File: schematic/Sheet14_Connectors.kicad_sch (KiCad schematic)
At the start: 5 parts, among them J1 JTAG, J2 SPW_TX, J3 SPW_RX, J4 POWER, J5 UART

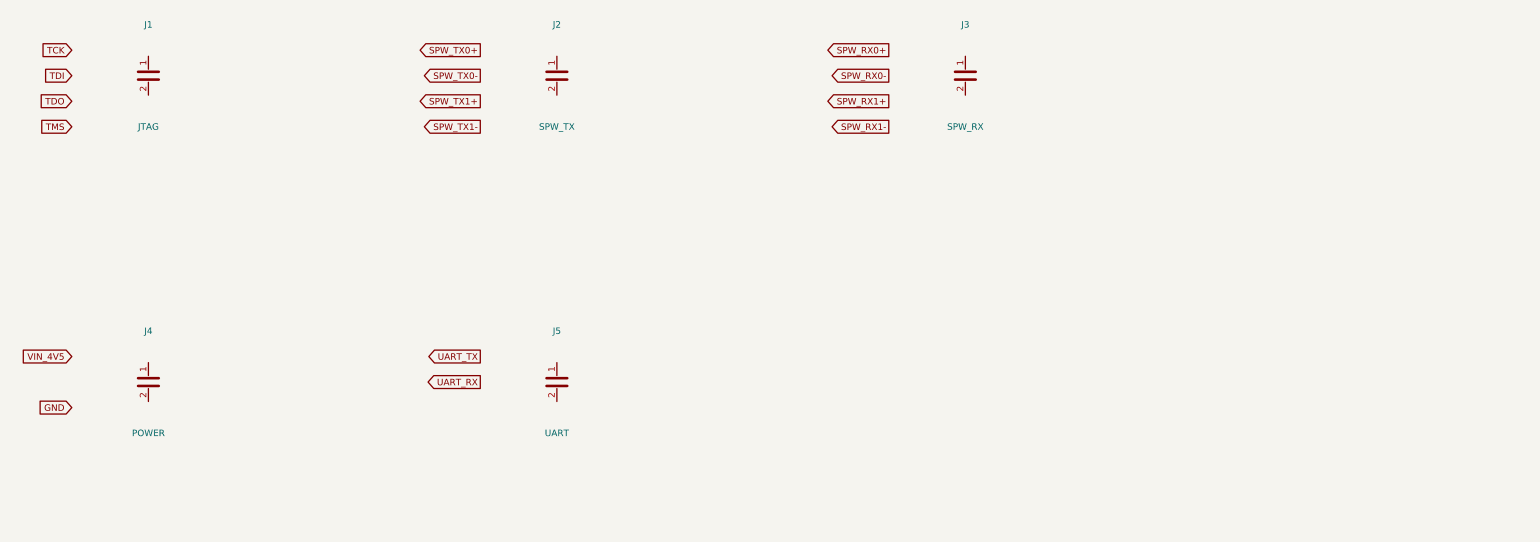
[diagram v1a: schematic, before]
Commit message: feat: schematic sheets with datasheet-correct IC pinouts and connections
- Downloaded 10 official datasheets (TI, Renesas, Crystek) for all major ICs
- Extracted exact pin configurations from PDF pin tables
- Generated Custom_ICs.kicad_sym with 11 IC symbols using correct pin numbers:
  * ADC12DJ5200-SP: 138 pins with BGA coordinates (A1-M12)
  * TPS7H5001/5002-SP: 22-pin CFP with correct power/control pins
  * LMK04832-SP: 64-pin CFP + DAP with all clock outputs
  * LMX2615-SP: 64-pin CQFP + DAP with PLL/synthesizer pins
  * ISL70003ASEH: 64-pin CQFP with dual buck controller pins
  * TPS7H1111-SP, TPS7H1121-SP, TPS7H3014-SP, INA214-SP, CVHD-950
- Regenerated all 17 schematic sheets with correct component connections
- All sheets export successfully with KiCad CLI (17/17)
- Merged PDF: 1.3MB, 17 pages
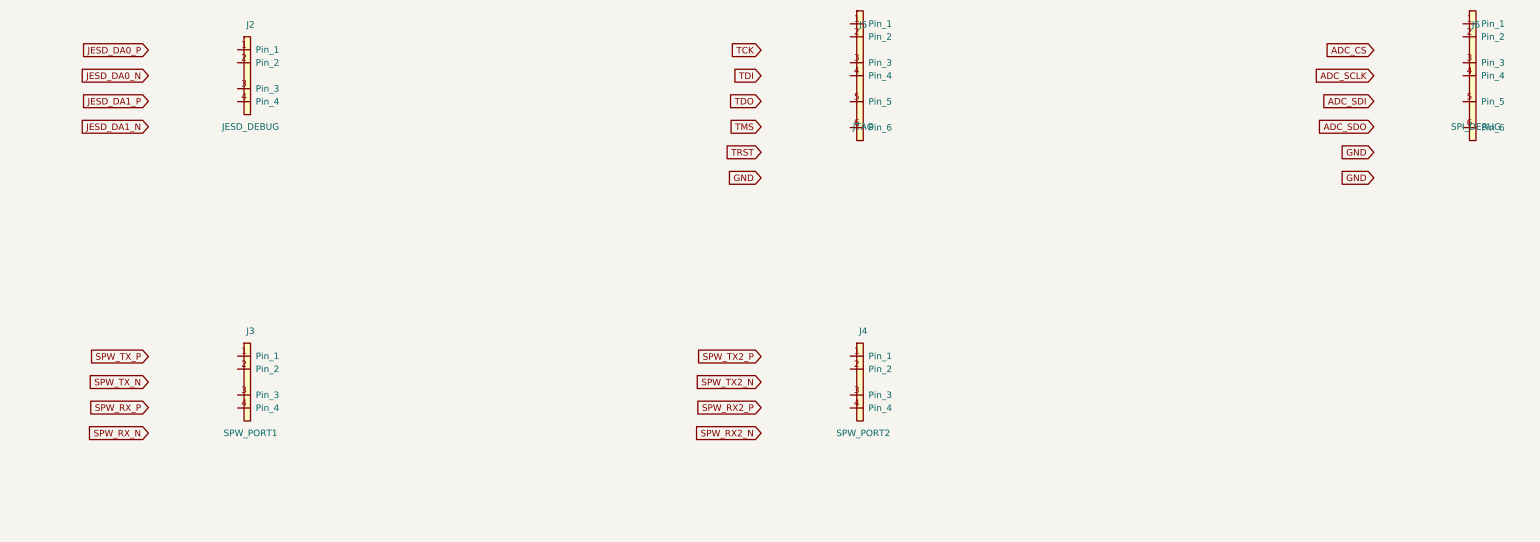
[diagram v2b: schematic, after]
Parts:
- removed J1: JTAG, Conn_01x06, symbol Device:C
- removed J2: SPW_TX, Conn_01x04, symbol Device:C
- removed J3: SPW_RX, Conn_01x04, symbol Device:C
- removed J4: POWER, Conn_01x02, symbol Device:C
- removed J5: UART, Conn_01x04, symbol Device:C
- added J2: JESD_DEBUG, Conn_01x04, symbol Connector:Conn_01x04
- added J3: SPW_PORT1, Conn_01x04, symbol Connector:Conn_01x04
- added J4: SPW_PORT2, Conn_01x04, symbol Connector:Conn_01x04
- added J5: JTAG, Conn_01x06, symbol Connector:Conn_01x06
- added J6: SPI_DEBUG, Conn_01x06, symbol Connector:Conn_01x06
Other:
- title: X-Band Digital Module 20x20cm -> X-Band Connectors
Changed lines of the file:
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@@
   (paper "A3")
   (title_block
-    (title "X-Band Digital Module 20x20cm")
+    (title "X-Band Connectors")
     (date "2026-09-10")
     (rev "1.0")
   )
-  (symbol (lib_id "Device:C") (at 60 60 0) (unit 1)
+  (symbol (lib_id "Connector:Conn_01x04") (at 80 60 0) (unit 1)
     (in_bom yes) (on_board yes)
-    (property "Reference" "J1" (at 60 50 0) (effects (font (size 1.27 1.27))))
-    (property "Value" "JTAG" (at 60 70 0) (effects (font (size 1.27 1.27))))
-    (property "Footprint" "Conn_01x06" (at 60 60 0) (effects (font (size 1.27 1.27)) hide))
+    (property "Reference" "J2" (at 80 50 0) (effects (font (size 1.27 1.27))))
+    (property "Value" "JESD_DEBUG" (at 80 70 0) (effects (font (size 1.27 1.27))))
+    (property "Footprint" "Conn_01x04" (at 80 60 0) (effects (font (size 1.27 1.27)) hide))
     (pin "1")
     (pin "2")
-  )
-  (symbol (lib_id "Device:C") (at 140 60 0) (unit 1)
+    (pin "3")
+    (pin "4")
+  )  (symbol (lib_id "Connector:Conn_01x04") (at 80 120 0) (unit 1)
     (in_bom yes) (on_board yes)
-    (property "Reference" "J2" (at 140 50 0) (effects (font (size 1.27 1.27))))
-    (property "Value" "SPW_TX" (at 140 70 0) (effects (font (size 1.27 1.27))))
-    (property "Footprint" "Conn_01x04" (at 140 60 0) (effects (font (size 1.27 1.27)) hide))
+    (property "Reference" "J3" (at 80 110 0) (effects (font (size 1.27 1.27))))
+    (property "Value" "SPW_PORT1" (at 80 130 0) (effects (font (size 1.27 1.27))))
+    (property "Footprint" "Conn_01x04" (at 80 120 0) (effects (font (size 1.27 1.27)) hide))
     (pin "1")
     (pin "2")
-  )
-  (symbol (lib_id "Device:C") (at 220 60 0) (unit 1)
+    (pin "3")
+    (pin "4")
+  )  (symbol (lib_id "Connector:Conn_01x04") (at 200 120 0) (unit 1)
     (in_bom yes) (on_board yes)
-    (property "Reference" "J3" (at 220 50 0) (effects (font (size 1.27 1.27))))
-    (property "Value" "SPW_RX" (at 220 70 0) (effects (font (size 1.27 1.27))))
-    (property "Footprint" "Conn_01x04" (at 220 60 0) (effects (font (size 1.27 1.27)) hide))
+    (property "Reference" "J4" (at 200 110 0) (effects (font (size 1.27 1.27))))
+    (property "Value" "SPW_PORT2" (at 200 130 0) (effects (font (size 1.27 1.27))))
+    (property "Footprint" "Conn_01x04" (at 200 120 0) (effects (font (size 1.27 1.27)) hide))
     (pin "1")
     (pin "2")
-  )
-  (symbol (lib_id "Device:C") (at 60 120 0) (unit 1)
+    (pin "3")
+    (pin "4")
+  )  (symbol (lib_id "Connector:Conn_01x06") (at 200 60 0) (unit 1)
     (in_bom yes) (on_board yes)
-    (property "Reference" "J4" (at 60 110 0) (effects (font (size 1.27 1.27))))
-    (property "Value" "POWER" (at 60 130 0) (effects (font (size 1.27 1.27))))
-    (property "Footprint" "Conn_01x02" (at 60 120 0) (effects (font (size 1.27 1.27)) hide))
+    (property "Reference" "J5" (at 200 50 0) (effects (font (size 1.27 1.27))))
+    (property "Value" "JTAG" (at 200 70 0) (effects (font (size 1.27 1.27))))
+    (property "Footprint" "Conn_01x06" (at 200 60 0) (effects (font (size 1.27 1.27)) hide))
     (pin "1")
     (pin "2")
-  )
-  (symbol (lib_id "Device:C") (at 140 120 0) (unit 1)
+    (pin "3")
+    (pin "4")
+    (pin "5")
+    (pin "6")
+  )  (symbol (lib_id "Connector:Conn_01x06") (at 320 60 0) (unit 1)
     (in_bom yes) (on_board yes)
-    (property "Reference" "J5" (at 140 110 0) (effects (font (size 1.27 1.27))))
-    (property "Value" "UART" (at 140 130 0) (effects (font (size 1.27 1.27))))
-    (property "Footprint" "Conn_01x04" (at 140 120 0) (effects (font (size 1.27 1.27)) hide))
+    (property "Reference" "J6" (at 320 50 0) (effects (font (size 1.27 1.27))))
+    (property "Value" "SPI_DEBUG" (at 320 70 0) (effects (font (size 1.27 1.27))))
+    (property "Footprint" "Conn_01x06" (at 320 60 0) (effects (font (size 1.27 1.27)) hide))
     (pin "1")
     (pin "2")
-  )
-  (global_label "TCK" (shape input) (at 45 55 180) (effects (font (size 1.27 1.27)) (justify right)))
-  (global_label "TDI" (shape input) (at 45 60 180) (effects (font (size 1.27 1.27)) (justify right)))
-  (global_label "TDO" (shape input) (at 45 65 180) (effects (font (size 1.27 1.27)) (justify right)))
-  (global_label "TMS" (shape input) (at 45 70 180) (effects (font (size 1.27 1.27)) (justify right)))
-  (global_label "SPW_TX0+" (shape output) (at 125 55 180) (effects (font (size 1.27 1.27)) (justify right)))
-  (global_label "SPW_TX0-" (shape output) (at 125 60 180) (effects (font (size 1.27 1.27)) (justify right)))
-  (global_label "SPW_TX1+" (shape output) (at 125 65 180) (effects (font (size 1.27 1.27)) (justify right)))
-  (global_label "SPW_TX1-" (shape output) (at 125 70 180) (effects (font (size 1.27 1.27)) (justify right)))
-  (global_label "SPW_RX0+" (shape output) (at 205 55 180) (effects (font (size 1.27 1.27)) (justify right)))
-  (global_label "SPW_RX0-" (shape output) (at 205 60 180) (effects (font (size 1.27 1.27)) (justify right)))
-  (global_label "SPW_RX1+" (shape output) (at 205 65 180) (effects (font (size 1.27 1.27)) (justify right)))
-  (global_label "SPW_RX1-" (shape output) (at 205 70 180) (effects (font (size 1.27 1.27)) (justify right)))
-  (global_label "VIN_4V5" (shape input) (at 45 115 180) (effects (font (size 1.27 1.27)) (justify right)))
-  (global_label "GND" (shape input) (at 45 125 180) (effects (font (size 1.27 1.27)) (justify right)))
-  (global_label "UART_TX" (shape output) (at 125 115 180) (effects (font (size 1.27 1.27)) (justify right)))
-  (global_label "UART_RX" (shape output) (at 125 120 180) (effects (font (size 1.27 1.27)) (justify right)))
-  (sheet_instances (path "/" (page "1")))
+    (pin "3")
+    (pin "4")
+    (pin "5")
+    (pin "6")
+  )  (global_label "JESD_DA0_P" (shape input) (at 60 55 180) (effects (font (size 1.27 1.27)) (justify right)))  (global_label "JESD_DA0_N" (shape input) (at 60 60 180) (effects (font (size 1.27 1.27)) (justify right)))  (global_label "JESD_DA1_P" (shape input) (at 60 65 180) (effects (font (size 1.27 1.27)) (justify right)))  (global_label "JESD_DA1_N" (shape input) (at 60 70 180) (effects (font (size 1.27 1.27)) (justify right)))  (global_label "SPW_TX_P" (shape input) (at 60 115 180) (effects (font (size 1.27 1.27)) (justify right)))  (global_label "SPW_TX_N" (shape input) (at 60 120 180) (effects (font (size 1.27 1.27)) (justify right)))  (global_label "SPW_RX_P" (shape input) (at 60 125 180) (effects (font (size 1.27 1.27)) (justify right)))  (global_label "SPW_RX_N" (shape input) (at 60 130 180) (effects (font (size 1.27 1.27)) (justify right)))  (global_label "SPW_TX2_P" (shape input) (at 180 115 180) (effects (font (size 1.27 1.27)) (justify right)))  (global_label "SPW_TX2_N" (shape input) (at 180 120 180) (effects (font (size 1.27 1.27)) (justify right)))  (global_label "SPW_RX2_P" (shape input) (at 180 125 180) (effects (font (size 1.27 1.27)) (justify right)))  (global_label "SPW_RX2_N" (shape input) (at 180 130 180) (effects (font (size 1.27 1.27)) (justify right)))  (global_label "TCK" (shape input) (at 180 55 180) (effects (font (size 1.27 1.27)) (justify right)))  (global_label "TDI" (shape input) (at 180 60 180) (effects (font (size 1.27 1.27)) (justify right)))  (global_label "TDO" (shape input) (at 180 65 180) (effects (font (size 1.27 1.27)) (justify right)))  (global_label "TMS" (shape input) (at 180 70 180) (effects (font (size 1.27 1.27)) (justify right)))  (global_label "TRST" (shape input) (at 180 75 180) (effects (font (size 1.27 1.27)) (justify right)))  (global_label "GND" (shape input) (at 180 80 180) (effects (font (size 1.27 1.27)) (justify right)))  (global_label "ADC_CS" (shape input) (at 300 55 180) (effects (font (size 1.27 1.27)) (justify right)))  (global_label "ADC_SCLK" (shape input) (at 300 60 180) (effects (font (size 1.27 1.27)) (justify right)))  (global_label "ADC_SDI" (shape input) (at 300 65 180) (effects (font (size 1.27 1.27)) (justify right)))  (global_label "ADC_SDO" (shape input) (at 300 70 180) (effects (font (size 1.27 1.27)) (justify right)))  (global_label "GND" (shape input) (at 300 75 180) (effects (font (size 1.27 1.27)) (justify right)))  (global_label "GND" (shape input) (at 300 80 180) (effects (font (size 1.27 1.27)) (justify right)))  (sheet_instances (path "/" (page "1")))
 )
